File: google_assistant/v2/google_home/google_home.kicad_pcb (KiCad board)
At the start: 2 copper layers, 70 x 25 mm, 22 parts, among them J1 Conn_01x16_MountingPin, J2 AudioJack2_SwitchT, J3 Conn_02x05_Odd_Even, J4 Conn_01x02, SW1 SW_SPDT, SW2 SW_SPDT, U1 R-78E5.0-1.0

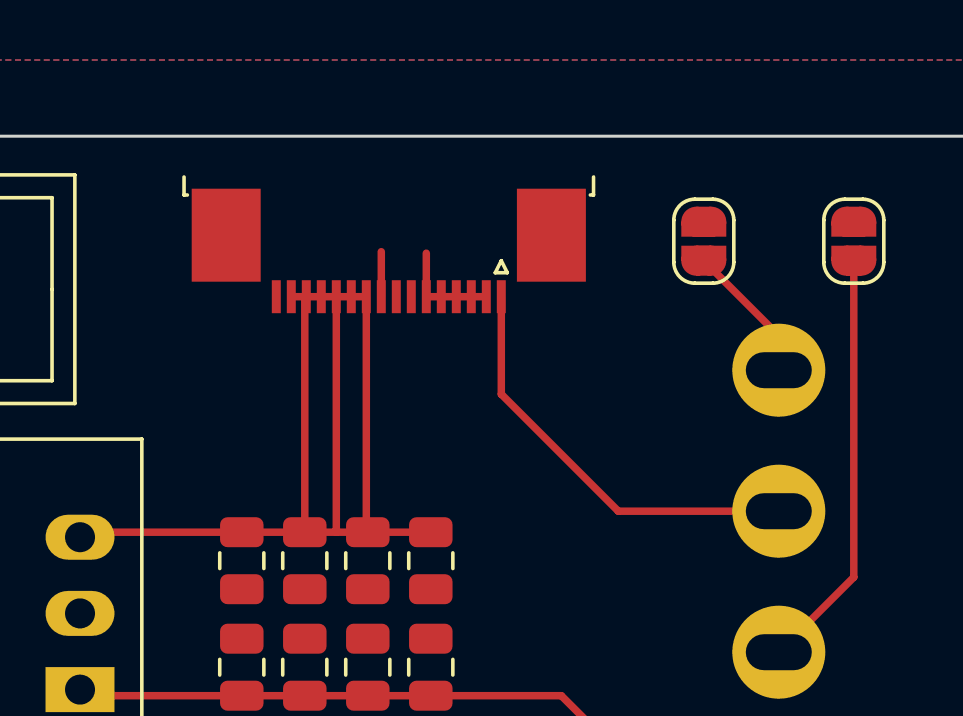
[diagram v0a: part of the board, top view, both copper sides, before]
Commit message: Fixed FFC connector footprint
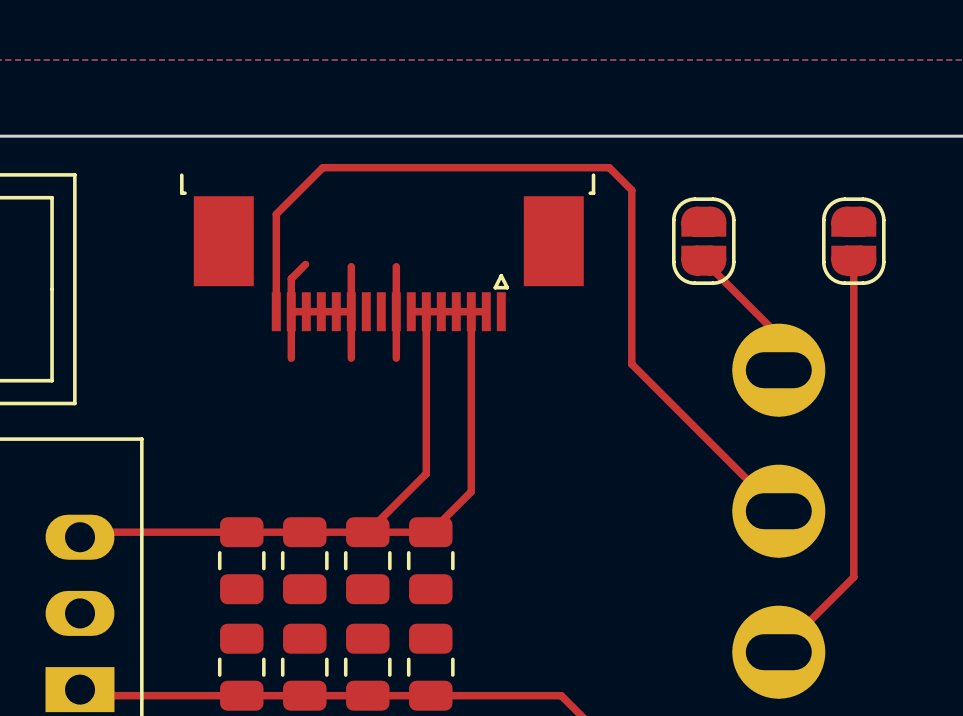
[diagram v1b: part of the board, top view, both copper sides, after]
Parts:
- moved J1 0.50 mm to (40.0, 4.50)
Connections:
- J1 pad 1: Net-(J1-Pin_1) -> unconnected-(J1-Pin_1-Pad1)
- J1 pad 10: +5V -> unconnected-(J1-Pin_10-Pad10)
- J1 pad 11: +5V -> GND
- J1 pad 12: +5V -> GND
- J1 pad 13: +5V -> GND
- J1 pad 14: +5V -> GND
- J1 pad 15: +5V -> GND
- J1 pad 16: unconnected-(J1-Pin_16-Pad16) -> Net-(J1-Pin_16)
- J1 pad 2: GND -> +5V
- J1 pad 3: GND -> +5V
- J1 pad 4: GND -> +5V
- J1 pad 5: GND -> +5V
- J1 pad 6: GND -> +5V
- J1 pad 7: unconnected-(J1-Pin_7-Pad7) -> +5V
- J1 pad 8: unconnected-(J1-Pin_8-Pad8) -> GND
- J1 pad 9: GND -> unconnected-(J1-Pin_9-Pad9)
- SW1 pad 2: Net-(J1-Pin_1) -> Net-(J1-Pin_16)
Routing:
- net Net-(J1-Pin_16): track 0.00 -> 28.8 mm
- net Net-(J1-Pin_1): track 14.1 -> 0.00 mm
- net +5V: track 37.9 -> 30.4 mm
- net GND: track 4.95 -> 11.4 mm

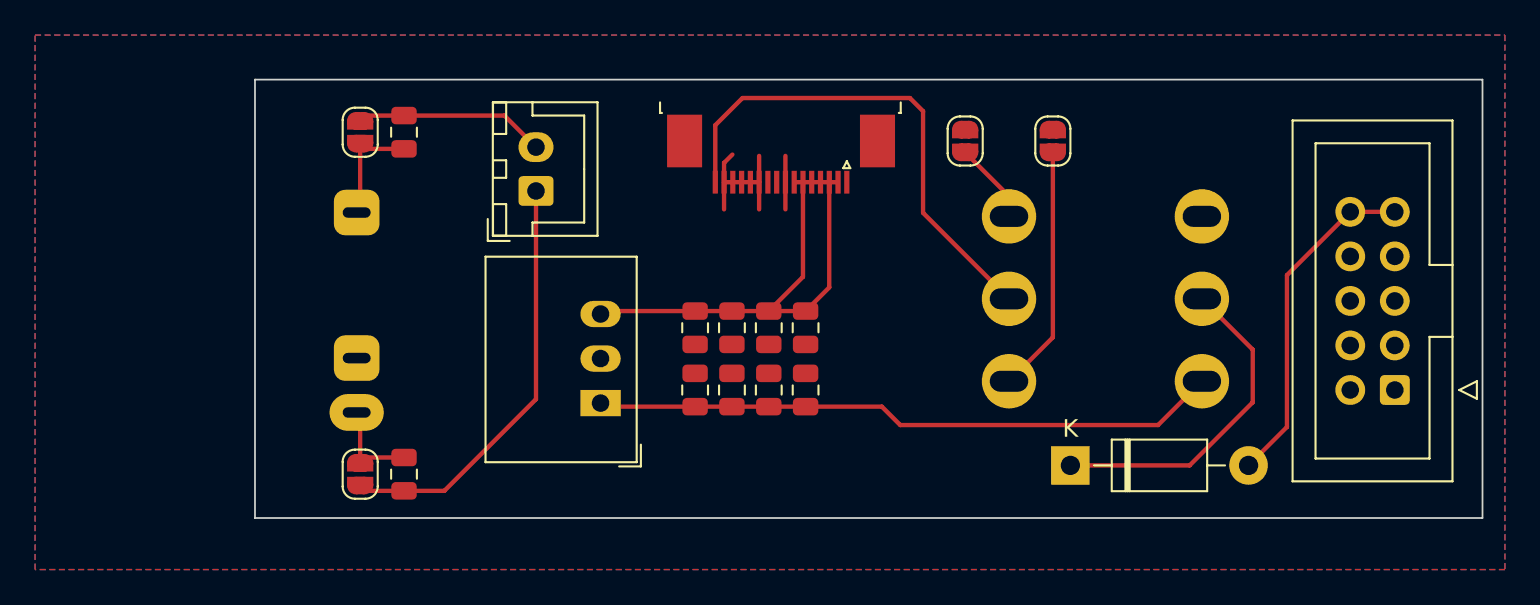
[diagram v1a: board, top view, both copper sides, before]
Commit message: Added transformer
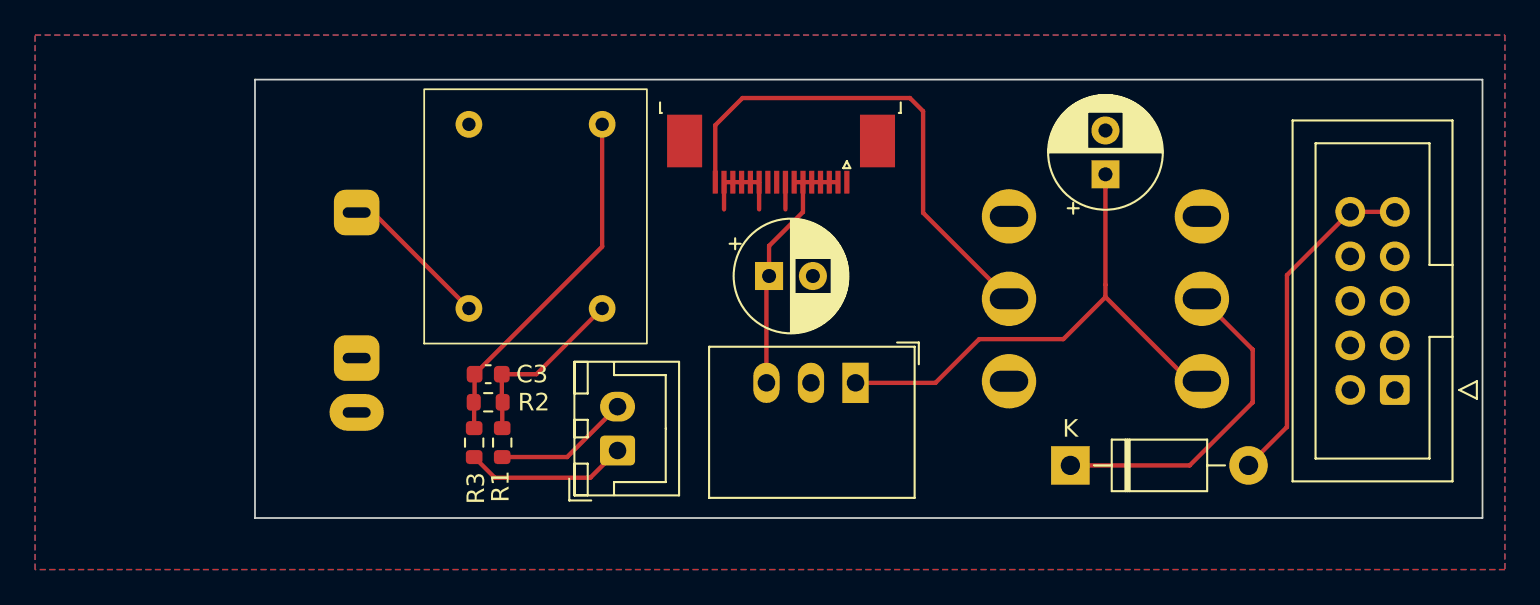
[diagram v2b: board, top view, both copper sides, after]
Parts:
- removed C10, C4, C5, C6, C7, C8, C9: 10u, Capacitor_SMD:C_0805_2012Metric
- removed JP1, JP2, JP3, JP4: SolderJumper_2_Open, Jumper:SolderJumper-2_P1.3mm_Open_RoundedPad1.0x1.5mm
- added R1: 1k, Resistor_SMD:R_0603_1608Metric, F.Cu at (24.1, 20.7)
- added R2: 200, Resistor_SMD:R_0603_1608Metric, F.Cu at (23.3, 18.4)
- added R3: 1k, Resistor_SMD:R_0603_1608Metric, F.Cu at (22.5, 20.7)
- added T1: Transformer_1P_1S, AlexCustom:EI14, F.Cu at (26.0, 7.80)
- C1, C2: value 10u -> 47u; footprint Capacitor_SMD:C_0805_2012Metric -> Capacitor_THT:CP_Radial_D6.3mm_P2.50mm
- C3: value 10u -> 10n; footprint Capacitor_SMD:C_0805_2012Metric -> Capacitor_SMD:C_0603_1608Metric
- moved C1 40.1 mm to (58.5, 5.40)
- moved C2 23.7 mm to (39.3, 11.2), turned to 0 degrees
- moved C3 16.2 mm to (23.3, 16.8), turned to 180 degrees
- moved J4 15.5 mm to (30.7, 21.1)
- moved U1 14.6 mm to (44.2, 17.3), turned to 180 degrees
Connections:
- C1 pad 1: Net-(JP2-A) -> +12V
- C1 pad 2: Net-(J4-Pin_2) -> GND
- C2 pad 1: Net-(JP1-B) -> +5V
- C2 pad 2: Net-(J4-Pin_1) -> GND
- C3 pad 1: GND -> Net-(T1-AA)
- C3 pad 2: +5V -> Net-(T1-AB)
- J2 pad S: Net-(JP1-B) -> GND
- J2 pad T: Net-(JP2-A) -> Net-(T1-SB)
- SW1 pad 1: Net-(JP3-A) -> unconnected-(SW1-A-Pad1)
- SW1 pad 3: Net-(JP4-B) -> GND
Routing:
- net Net-(T1-AB): track 0.00 -> 20.4 mm
- net +5V: track 30.4 -> 14.8 mm
- net Net-(J4-Pin_1): track 24.2 -> 9.30 mm
- net Net-(JP3-A): track 14.1 -> 0.00 mm
- net Net-(T1-AA): track 0.00 -> 10.4 mm
- net Net-(T1-SB): track 0.00 -> 8.67 mm
- net Net-(JP2-A): track 6.64 -> 0.00 mm
- net Net-(JP1-B): track 5.58 -> 0.00 mm
- net +12V: track 35.8 -> 30.8 mm
- net GND: track 11.4 -> 6.65 mm
- net Net-(JP4-B): track 4.69 -> 0.00 mm
- net Net-(J4-Pin_2): track 10.9 -> 7.77 mm

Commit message: Simplified schematic
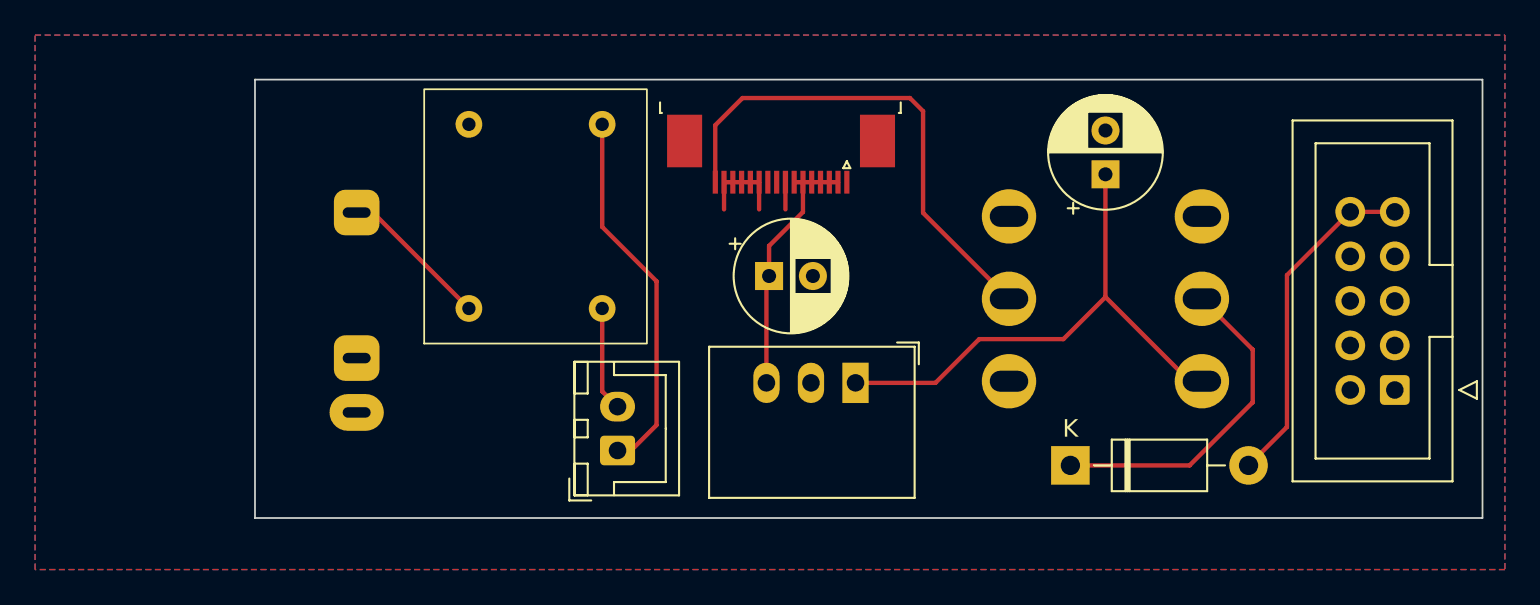
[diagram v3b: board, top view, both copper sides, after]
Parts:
- removed C3: 10n, Capacitor_SMD:C_0603_1608Metric
- removed R1, R3: 1k, Resistor_SMD:R_0603_1608Metric
- removed R2: 200, Resistor_SMD:R_0603_1608Metric
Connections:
- T1 pad 1: Net-(T1-AA) -> Net-(J4-Pin_2)
- T1 pad 2: Net-(T1-AB) -> Net-(J4-Pin_1)
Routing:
- net Net-(T1-AB): track 20.4 -> 0.00 mm
- net Net-(J4-Pin_1): track 9.30 -> 21.3 mm
- net Net-(T1-AA): track 10.4 -> 0.00 mm
- net Net-(J4-Pin_2): track 7.77 -> 5.96 mm

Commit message: Updated trace widths and capacitor values
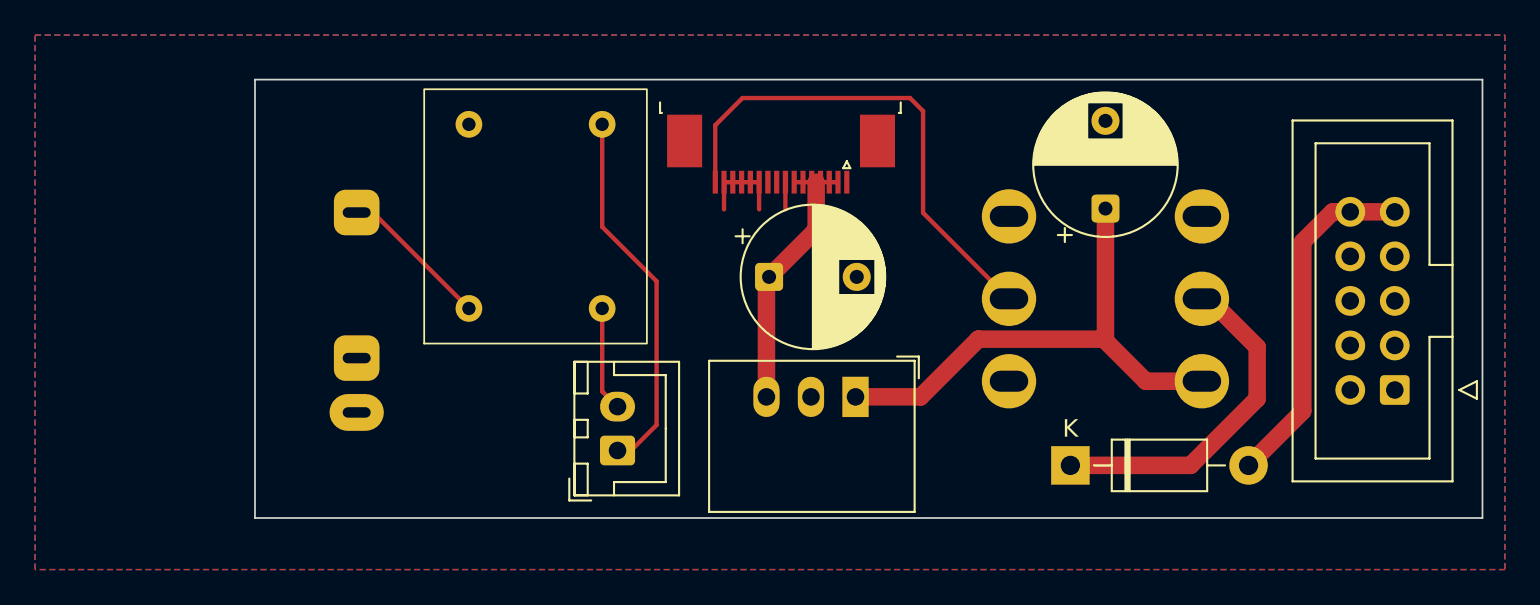
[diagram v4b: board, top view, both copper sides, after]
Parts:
- C1: value 47u -> 330u; footprint Capacitor_THT:CP_Radial_D6.3mm_P2.50mm -> Capacitor_THT:CP_Radial_D8.0mm_P5.00mm
- C2: value 47u -> 1000u; footprint Capacitor_THT:CP_Radial_D6.3mm_P2.50mm -> Capacitor_THT:CP_Radial_D8.0mm_P5.00mm
- moved C1 1.95 mm to (58.5, 7.35)
- moved U1 0.80 mm to (44.2, 18.1)
- moved C2 0.05 mm to (39.3, 11.2)
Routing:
- net +5V: track 14.8 -> 15.9 mm
- net +12V: track 30.8 -> 29.7 mm
- net Net-(D2-A): track 19.4 -> 20.0 mm
